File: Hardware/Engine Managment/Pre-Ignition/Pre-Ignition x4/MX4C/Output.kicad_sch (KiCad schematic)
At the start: 19 parts, among them Q5 AO3400A, Q6 AO3400A, Q7 AO3400A, Q8 AO3400A, U6 ULN2003A

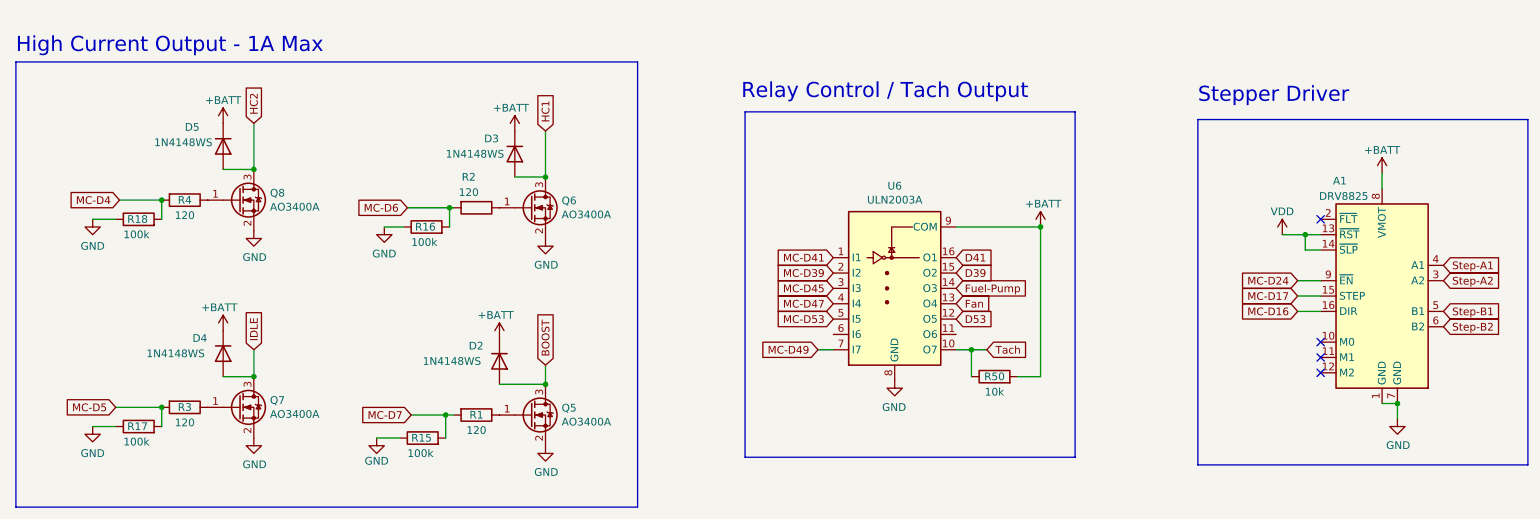
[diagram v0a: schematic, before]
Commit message: Upload correct initial upload files
Initial upload files were accidently taken from an alpha folder. 5v pins on main connector had no voltage. To fix the issue on any manufactured boards remove C8 and C9. Then short the pins of the removed capacitors.
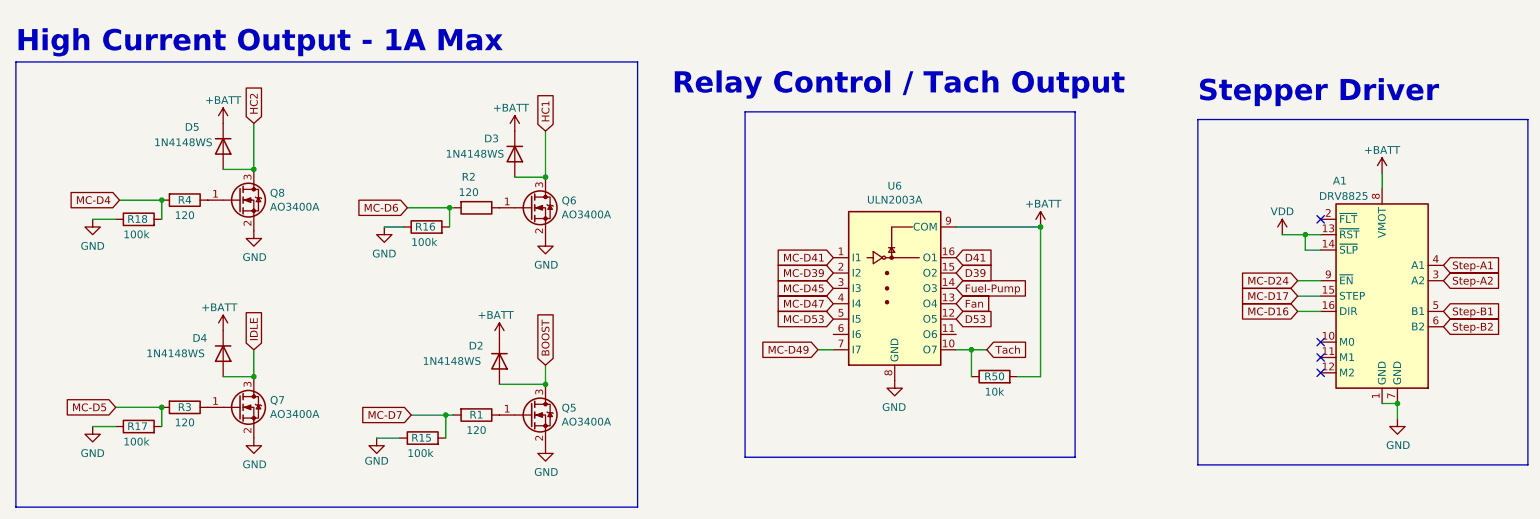
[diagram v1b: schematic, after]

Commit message: Structure Update
MX2 - RevB Upload
MX4B-2 - KiCad Version update (no changes)
MX4C - Organized Schematic, Minor layout change
Engine Simulator 8 Channel - Organized Schematic (no changes)
PMAP-M - Map Sensor Breakout for MX4C
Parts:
- A1: footprint Module:Pololu_Breakout-16_15.2x20.3mm -> Detonation:DVR8825-Labeled-Front
- R10: renamed from R4; value 120 -> 470r; LCSC C25079 -> C25117
- R7: renamed from R1; value 120 -> 470r; LCSC C25079 -> C25117
- R8: renamed from R2; value 120 -> 470r; LCSC C25079 -> C25117
- R9: renamed from R3; value 120 -> 470r; LCSC C25079 -> C25117
- renumbered D2 to D3, D3 to D4, D4 to D5, D5 to D6, R50 to R51
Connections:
- net VDD renamed +5V
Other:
- note added: "Relay Control Tach Output"
- note removed: "Relay Control / Tach Output"
- moved on the sheet: A1, D3, D4, D5, D6, Q5, Q6, Q7, Q8, R10, R15, R16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

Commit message: minor update
Copper Pour and clearances updated.
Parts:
- renumbered D3 to D4, D4 to D5, D5 to D6, D6 to D7, R51 to R52, U6 to U5
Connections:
- net D53: now also U5.11 (O6)
- net MC-D53: now also U5.6 (I6)
- net HC1 renamed IDLE2
- net HC2 renamed VVT
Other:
- note added: "HC1"
- note added: "HC2"
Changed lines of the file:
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@@
   (title_block
     (title "Pre-Ignition X4")
-    (date "2023-06-15")
+    (date "2023-10-24")
     (rev "C")
     (company "DetonationEMS")
@@
     (stroke (width 0) (type default))
   )
+  (wire (pts (xy 152.4 102.87) (xy 154.94 102.87))
+    (stroke (width 0) (type default))
+  )
   (wire (pts (xy 236.22 115.57) (xy 236.22 118.11))
     (stroke (width 0) (type default))
@@
     (stroke (width 0) (type default))
   )
+  (wire (pts (xy 152.4 102.87) (xy 152.4 105.41))
+    (stroke (width 0) (type default))
+  )
   (wire (pts (xy 96.52 124.46) (xy 96.52 128.27))
     (stroke (width 0) (type default))
@@
     (stroke (width 0) (type default))
   )
+  (wire (pts (xy 154.94 105.41) (xy 152.4 105.41))
+    (stroke (width 0) (type default))
+  )
   (wire (pts (xy 113.03 115.57) (xy 113.03 119.38))
     (stroke (width 0) (type default))
@@
     (stroke (width 0) (type default))
   )
+  (wire (pts (xy 177.8 102.87) (xy 177.8 105.41))
+    (stroke (width 0) (type default))
+  )
+  (wire (pts (xy 177.8 105.41) (xy 175.26 105.41))
+    (stroke (width 0) (type default))
+  )
   (wire (pts (xy 107.95 85.09) (xy 113.03 85.09))
     (stroke (width 0) (type default))
@@
   )
   (wire (pts (xy 219.71 95.25) (xy 223.52 95.25))
+    (stroke (width 0) (type default))
+  )
+  (wire (pts (xy 175.26 102.87) (xy 177.8 102.87))
     (stroke (width 0) (type default))
   )
@@
   (text "High Current Output - 1A Max" (at 26.67 67.31 0)
     (effects (font (size 3.5 3.5) (thickness 0.7) bold) (justify left bottom))
+  )
+  (text "HC2" (at 66.04 76.835 0)
+    (effects (font (size 1.27 1.27)) (justify left bottom))
+  )
+  (text "HC1" (at 114.935 78.105 0)
+    (effects (font (size 1.27 1.27)) (justify left bottom))
   )
   (text "Relay Control\nTach Output" (at 142.24 71.12 0)
@@
     )
   )
-  (global_label "MC-D53" (shape input) (at 154.94 102.87 180) (fields_autoplaced)
+  (global_label "MC-D53" (shape input) (at 152.4 104.14 180) (fields_autoplaced)
     (effects (font (size 1.27 1.27)) (justify right))
-    (property "Intersheetrefs" "${INTERSHEET_REFS}" (at -54.61 48.26 0)
+    (property "Intersheetrefs" "${INTERSHEET_REFS}" (at -57.15 49.53 0)
       (effects (font (size 1.27 1.27)) hide)
     )
@@
     )
   )
-  (global_label "D53" (shape input) (at 175.26 102.87 0) (fields_autoplaced)
-    (effects (font (size 1.27 1.27)) (justify left))
-    (property "Intersheetrefs" "${INTERSHEET_REFS}" (at -54.61 48.26 0)
+  (global_label "D53" (shape input) (at 177.8 104.14 0) (fields_autoplaced)
+    (effects (font (size 1.27 1.27)) (justify left))
+    (property "Intersheetrefs" "${INTERSHEET_REFS}" (at -52.07 49.53 0)
       (effects (font (size 1.27 1.27)) hide)
     )
@@
     )
   )
-  (global_label "HC1" (shape input) (at 113.03 80.01 0) (fields_autoplaced)
-    (effects (font (size 1.27 1.27)) (justify left))
-    (property "Intersheetrefs" "${INTERSHEET_REFS}" (at 119.0916 80.01 0)
+  (global_label "IDLE2" (shape input) (at 113.03 80.01 0) (fields_autoplaced)
+    (effects (font (size 1.27 1.27)) (justify left))
+    (property "Intersheetrefs" "${INTERSHEET_REFS}" (at 120.6224 80.01 0)
       (effects (font (size 1.27 1.27)) (justify left) hide)
     )
@@
     )
   )
-  (global_label "HC2" (shape input) (at 64.77 78.74 0) (fields_autoplaced)
-    (effects (font (size 1.27 1.27)) (justify left))
-    (property "Intersheetrefs" "${INTERSHEET_REFS}" (at 70.8316 78.74 0)
+  (global_label "VVT" (shape input) (at 64.77 78.74 0) (fields_autoplaced)
+    (effects (font (size 1.27 1.27)) (justify left))
+    (property "Intersheetrefs" "${INTERSHEET_REFS}" (at 70.2458 78.74 0)
       (effects (font (size 1.27 1.27)) (justify left) hide)
     )
@@
   (symbol (lib_id "Transistor_Array:ULN2003A") (at 165.1 97.79 0) (unit 1)
     (in_bom yes) (on_board yes) (dnp no)
-    (property "Reference" "U6" (at 165.1 80.8482 0)
+    (property "Reference" "U5" (at 165.1 80.8482 0)
       (effects (font (size 1.27 1.27)))
     )
@@
       (project "Pre_Ignition"
         (path "/929a9b03-e99e-4b88-8e16-759f8c6b59a5/00000000-0000-0000-0000-000060e7aa2a"
-          (reference "U6") (unit 1)
+          (reference "U5") (unit 1)
         )
       )
@@
   (symbol (lib_id "Diode:1N4148WS") (at 105.41 115.57 270) (unit 1)
     (in_bom yes) (on_board yes) (dnp no)
-    (property "Reference" "D3" (at 100.33 113.03 90)
+    (property "Reference" "D4" (at 100.33 113.03 90)
       (effects (font (size 1.27 1.27)) (justify left))
     )
@@
       (project "Pre_Ignition"
         (path "/929a9b03-e99e-4b88-8e16-759f8c6b59a5/00000000-0000-0000-0000-000060e7aa2a"
-          (reference "D3") (unit 1)
+          (reference "D4") (unit 1)
         )
       )
@@
   (symbol (lib_id "Diode:1N4148WS") (at 107.95 81.28 270) (unit 1)
     (in_bom yes) (on_board yes) (dnp no)
-    (property "Reference" "D4" (at 102.87 78.74 90)
+    (property "Reference" "D5" (at 102.87 78.74 90)
       (effects (font (size 1.27 1.27)) (justify left))
     )
@@
       (project "Pre_Ignition"
         (path "/929a9b03-e99e-4b88-8e16-759f8c6b59a5/00000000-0000-0000-0000-000060e7aa2a"
-          (reference "D4") (unit 1)
+          (reference "D5") (unit 1)
         )
       )
@@
   (symbol (lib_id "Diode:1N4148WS") (at 59.69 80.01 270) (unit 1)
     (in_bom yes) (on_board yes) (dnp no)
-    (property "Reference" "D6" (at 53.34 76.835 90)
+    (property "Reference" "D7" (at 53.34 76.835 90)
       (effects (font (size 1.27 1.27)) (justify left))
     )
@@
       (project "Pre_Ignition"
         (path "/929a9b03-e99e-4b88-8e16-759f8c6b59a5/00000000-0000-0000-0000-000060e7aa2a"
+          (reference "D7") (unit 1)
+        )
+      )
+    )
+  )
+  (symbol (lib_id "power:+BATT") (at 59.69 76.2 0) (unit 1)
+    (in_bom yes) (on_board yes) (dnp no)
+    (property "Reference" "#PWR03" (at 59.69 80.01 0)
+      (effects (font (size 1.27 1.27)) hide)
+    )
+    (property "Value" "+BATT" (at 59.69 72.39 0)
+      (effects (font (size 1.27 1.27)))
+    )
+    (property "Footprint" "" (at 59.69 76.2 0)
+      (effects (font (size 1.27 1.27)) hide)
+    )
+    (property "Datasheet" "" (at 59.69 76.2 0)
+      (effects (font (size 1.27 1.27)) hide)
+    )
+    (pin "1")
+    (instances
+      (project "Pre_Ignition"
+        (path "/929a9b03-e99e-4b88-8e16-759f8c6b59a5/00000000-0000-0000-0000-000060e7aa2a"
+          (reference "#PWR03") (unit 1)
+        )
+      )
+    )
+  )
+  (symbol (lib_id "Diode:1N4148WS") (at 59.69 114.3 270) (unit 1)
+    (in_bom yes) (on_board yes) (dnp no)
+    (property "Reference" "D6" (at 54.61 111.76 90)
+      (effects (font (size 1.27 1.27)) (justify left))
+    )
+    (property "Value" "1N4148WS" (at 46.99 114.3 90)
+      (effects (font (size 1.27 1.27)) (justify left))
+    )
+    (property "Footprint" "Diode_SMD:D_SOD-323F" (at 59.69 114.3 0)
+      (effects (font (size 1.27 1.27)) hide)
+    )
+    (property "Datasheet" "https://www.vishay.com/docs/85751/1n4148ws.pdf" (at 59.69 114.3 0)
+      (effects (font (size 1.27 1.27)) hide)
+    )
+    (property "JLC" "C2128" (at 59.69 114.3 0)
+      (effects (font (size 1.27 1.27)) hide)
+    )
+    (property "LCSC" "C2128" (at 59.69 114.3 0)
+      (effects (font (size 1.27 1.27)) hide)
+    )
+    (pin "1")
+    (pin "2")
+    (instances
+      (project "Pre_Ignition"
+        (path "/929a9b03-e99e-4b88-8e16-759f8c6b59a5/00000000-0000-0000-0000-000060e7aa2a"
           (reference "D6") (unit 1)
-        )
-      )
-    )
-  )
-  (symbol (lib_id "power:+BATT") (at 59.69 76.2 0) (unit 1)
-    (in_bom yes) (on_board yes) (dnp no)
-    (property "Reference" "#PWR03" (at 59.69 80.01 0)
-      (effects (font (size 1.27 1.27)) hide)
-    )
-    (property "Value" "+BATT" (at 59.69 72.39 0)
-      (effects (font (size 1.27 1.27)))
-    )
-    (property "Footprint" "" (at 59.69 76.2 0)
-      (effects (font (size 1.27 1.27)) hide)
-    )
-    (property "Datasheet" "" (at 59.69 76.2 0)
-      (effects (font (size 1.27 1.27)) hide)
-    )
-    (pin "1")
-    (instances
-      (project "Pre_Ignition"
-        (path "/929a9b03-e99e-4b88-8e16-759f8c6b59a5/00000000-0000-0000-0000-000060e7aa2a"
-          (reference "#PWR03") (unit 1)
-        )
-      )
-    )
-  )
-  (symbol (lib_id "Diode:1N4148WS") (at 59.69 114.3 270) (unit 1)
-    (in_bom yes) (on_board yes) (dnp no)
-    (property "Reference" "D5" (at 54.61 111.76 90)
-      (effects (font (size 1.27 1.27)) (justify left))
-    )
-    (property "Value" "1N4148WS" (at 46.99 114.3 90)
-      (effects (font (size 1.27 1.27)) (justify left))
-    )
-    (property "Footprint" "Diode_SMD:D_SOD-323F" (at 59.69 114.3 0)
-      (effects (font (size 1.27 1.27)) hide)
-    )
-    (property "Datasheet" "https://www.vishay.com/docs/85751/1n4148ws.pdf" (at 59.69 114.3 0)
-      (effects (font (size 1.27 1.27)) hide)
-    )
-    (property "JLC" "C2128" (at 59.69 114.3 0)
-      (effects (font (size 1.27 1.27)) hide)
-    )
-    (property "LCSC" "C2128" (at 59.69 114.3 0)
-      (effects (font (size 1.27 1.27)) hide)
-    )
-    (pin "1")
-    (pin "2")
-    (instances
-      (project "Pre_Ignition"
-        (path "/929a9b03-e99e-4b88-8e16-759f8c6b59a5/00000000-0000-0000-0000-000060e7aa2a"
-          (reference "D5") (unit 1)
         )
       )
@@
   (symbol (lib_id "Device:R") (at 181.61 112.395 90) (unit 1)
     (in_bom yes) (on_board yes) (dnp no)
-    (property "Reference" "R51" (at 181.61 112.395 90)
+    (property "Reference" "R52" (at 181.61 112.395 90)
       (effects (font (size 1.27 1.27)))
     )
@@
       (project "Pre_Ignition"
         (path "/929a9b03-e99e-4b88-8e16-759f8c6b59a5/00000000-0000-0000-0000-000060e7aa2a"
-          (reference "R51") (unit 1)
-        )
-      )
+          (reference "R52") (unit 1)
+        )
+      )
